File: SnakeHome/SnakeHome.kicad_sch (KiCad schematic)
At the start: 4 parts, among them J1 Raspberry_Pi_4, U1 Temp&Humidity, U2 PIR_motion, U3 16_channel_relay

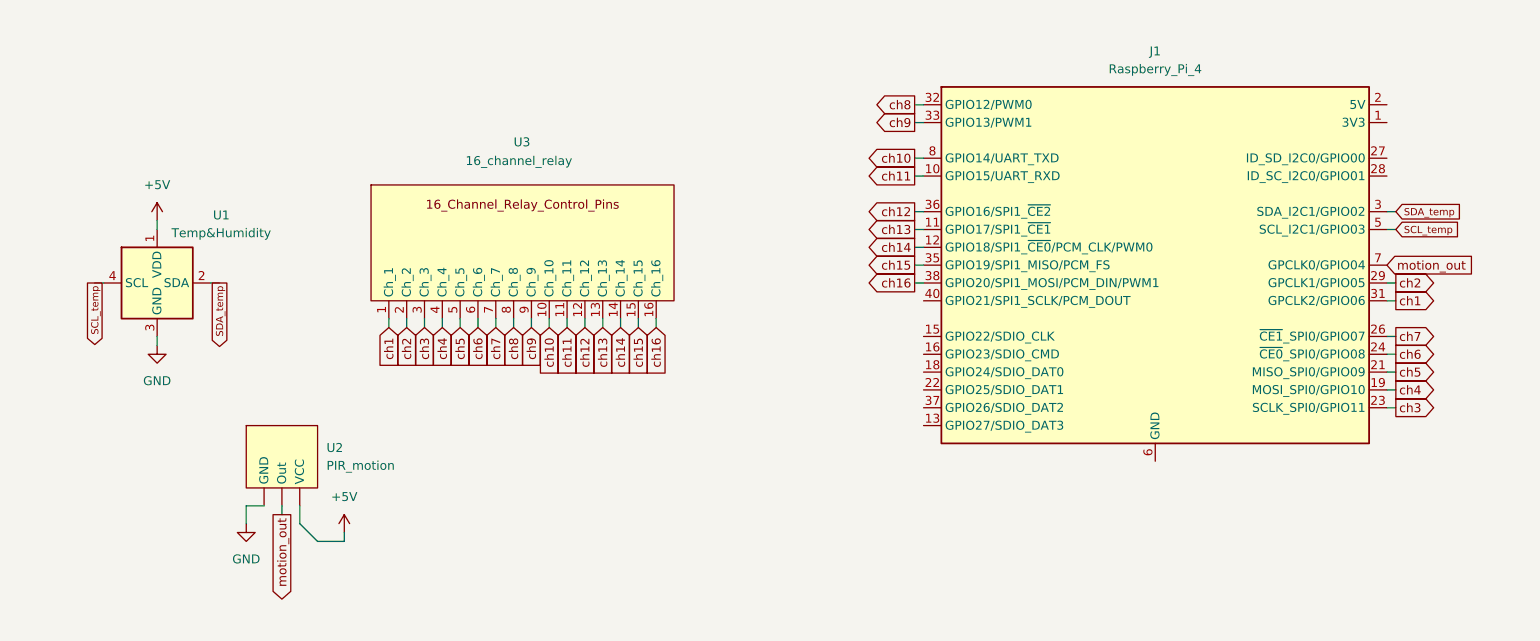
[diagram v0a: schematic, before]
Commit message: Finished the PCB hat
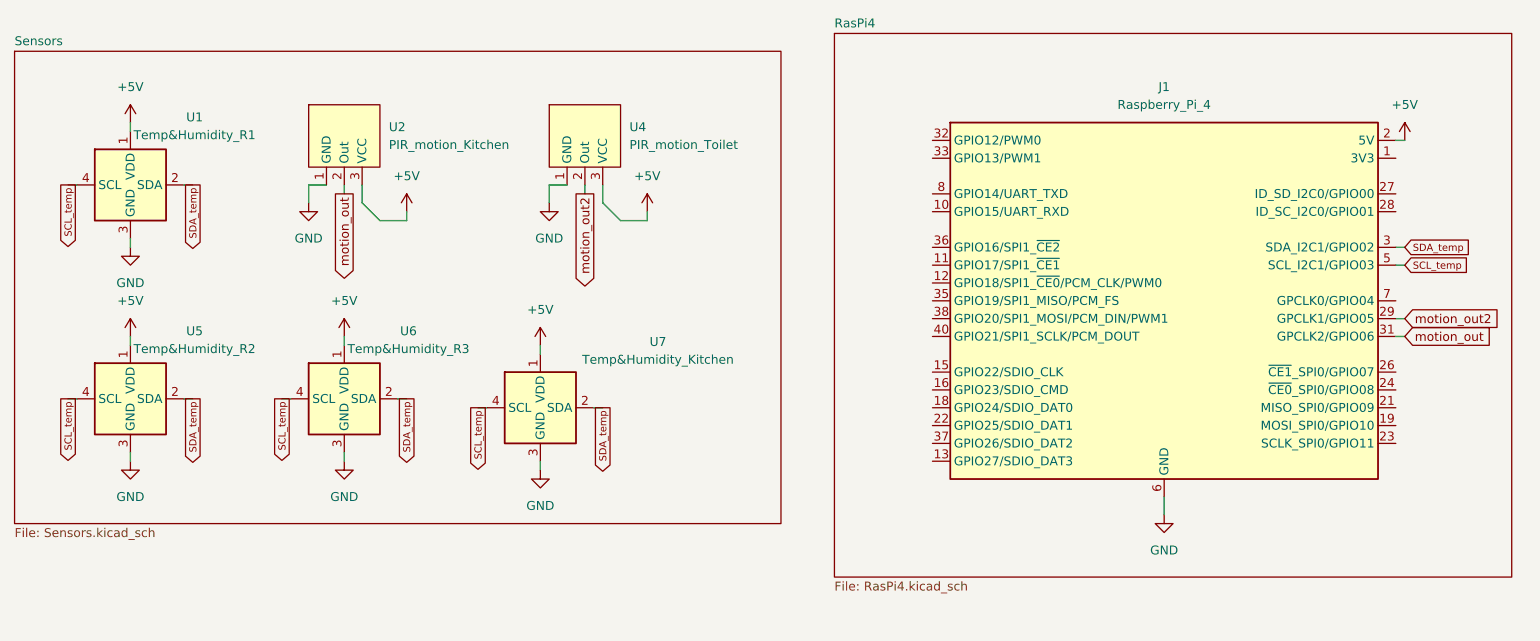
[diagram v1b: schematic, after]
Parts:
- removed U3: 16_channel_relay, symbol RAM-Components:16_relay
- added U4: PIR_motion_Toilet, Connector_PinHeader_2.54mm:PinHeader_1x03_P2.54mm_Vertical, symbol RAM-Components:PIR_motion
- added U5: Temp&Humidity_R2, Connector_PinHeader_2.54mm:PinHeader_1x04_P2.54mm_Vertical, symbol Sensor:AM2302
- added U6: Temp&Humidity_R3, Connector_PinHeader_2.54mm:PinHeader_1x04_P2.54mm_Vertical, symbol Sensor:AM2302
- added U7: Temp&Humidity_Kitchen, Connector_PinHeader_2.54mm:PinHeader_1x04_P2.54mm_Vertical, symbol Sensor:AM2302
- J1: footprint (none) -> Connector_PinSocket_2.54mm:PinSocket_2x20_P2.54mm_Vertical
- U1: value Temp&Humidity -> Temp&Humidity_R1
- U2: value PIR_motion -> PIR_motion_Kitchen; footprint (none) -> Connector_PinHeader_2.54mm:PinHeader_1x03_P2.54mm_Vertical
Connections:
- net ch1 is gone; now on net motion_out: J1.31 (GPCLK2/GPIO06)
- net +5V: now also J1.2 (5V), J1.4 (5V), U2.3 (VCC), U4.3 (VCC), U5.1 (VDD), U6.1 (VDD), U7.1 (VDD); no longer U2. (VCC)
- net GND: now also J1.14 (GND), J1.20 (GND), J1.25 (GND), J1.30 (GND), J1.34 (GND), J1.39 (GND), J1.6 (GND), J1.9 (GND), U2.1 (GND), U4.1 (GND), U5.3 (GND), U6.3 (GND), U7.3 (GND); no longer U2. (VCC)
- net SCL_temp: now also U5.4 (SCL), U6.4 (SCL), U7.4 (SCL)
- net SDA_temp: now also U5.2 (SDA), U6.2 (SDA), U7.2 (SDA)
- net motion_out: now also U2.2 (Out); no longer J1.7 (GPCLK0/GPIO04), U2. (VCC)
- net ch10: no longer names the net of J1.8 (GPIO14/UART_TXD)
- net ch11: no longer names the net of J1.10 (GPIO15/UART_RXD)
- net ch12: no longer names the net of J1.36 (GPIO16/SPI1_~{CE2})
- net ch13: no longer names the net of J1.11 (GPIO17/SPI1_~{CE1})
- net ch14: no longer names the net of J1.12 (GPIO18/SPI1_~{CE0}/PCM_CLK/PWM0)
- net ch15: no longer names the net of J1.35 (GPIO19/SPI1_MISO/PCM_FS)
- net ch16: no longer names the net of J1.38 (GPIO20/SPI1_MOSI/PCM_DIN/PWM1)
- net ch2 renamed motion_out2
- net motion_out2: now also U4.2 (Out)
- net ch3: no longer names the net of J1.23 (SCLK_SPI0/GPIO11)
- net ch4: no longer names the net of J1.19 (MOSI_SPI0/GPIO10)
- net ch5: no longer names the net of J1.21 (MISO_SPI0/GPIO09)
- net ch6: no longer names the net of J1.24 (~{CE0}_SPI0/GPIO08)
- net ch7: no longer names the net of J1.26 (~{CE1}_SPI0/GPIO07)
- net ch8: no longer names the net of J1.32 (GPIO12/PWM0)
- net ch9: no longer names the net of J1.33 (GPIO13/PWM1)
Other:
- added sheet RasPi4 (RasPi4.kicad_sch)
- added sheet Sensors (Sensors.kicad_sch)
- moved on the sheet: J1, U1
